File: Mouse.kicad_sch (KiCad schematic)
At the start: 0 parts

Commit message: putting onto other computers
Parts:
- added C1, C10, C11, C12, C13, C14, C4, C5, C6, C7, C8, C9: 100nF, symbol Device:C
- added R1, R2: 27.4, symbol Device:R
- added U1: RP2040, Package_DFN_QFN:QFN-56-1EP_7x7mm_P0.4mm_EP3.2x3.2mm, symbol MCU_RaspberryPi:RP2040
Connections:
- new net: R2.2, U1.46 (USB_DM)
- new net: R1.2, U1.47 (USB_DP)
- new net: U1.1 (IOVDD), U1.10 (IOVDD), U1.22 (IOVDD), U1.33 (IOVDD), U1.42 (IOVDD), U1.43 (ADC_AVDD), U1.44 (VREG_VIN), U1.48 (USB_VDD), U1.49 (IOVDD)
- new net: U1.23 (DVDD), U1.45 (VREG_VOUT), U1.50 (DVDD)
- new net +1V1: C10.1, C11.1, C12.1
- new net +3V3: C1.1, C13.1, C14.1, C4.1, C5.1, C6.1, C7.1, C8.1, C9.1
- new net ADC0: U1.38 (GPIO26/ADC0)
- new net ADC1: U1.39 (GPIO27/ADC1)
- new net ADC2: U1.40 (GPIO28/ADC2)
- new net ADC3: U1.41 (GPIO29/ADC3)
- new net GND: C1.2, C10.2, C11.2, C12.2, C13.2, C14.2, C4.2, C5.2, C6.2, C7.2, C8.2, C9.2, U1.57 (GND)
- new net I001: U1.3 (GPIO1)
- new net I002: U1.4 (GPIO2)
- new net IO00: U1.2 (GPIO0)
- new net IO03: U1.5 (GPIO3)
- new net IO04: U1.6 (GPIO4)
- new net IO05: U1.7 (GPIO5)
- new net IO06: U1.8 (GPIO6)
- new net IO07: U1.9 (GPIO7)
- new net IO08: U1.11 (GPIO8)
- new net IO09: U1.12 (GPIO9)
- new net IO10: U1.13 (GPIO10)
- new net IO11: U1.14 (GPIO11)
- new net IO12: U1.15 (GPIO12)
- new net IO13: U1.16 (GPIO13)
- new net IO14: U1.17 (GPIO14)
- new net IO15: U1.18 (GPIO15)
- new net IO16: U1.27 (GPIO16)
- new net IO17: U1.28 (GPIO17)
- new net IO18: U1.29 (GPIO18)
- new net IO19: U1.30 (GPIO19)
- new net IO20: U1.31 (GPIO20)
- new net IO21: U1.32 (GPIO21)
- new net IO22: U1.34 (GPIO22)
- new net IO23: U1.35 (GPIO23)
- new net IO24: U1.36 (GPIO24)
- new net IO25: U1.37 (GPIO25)
- new net QSPL_SCLK: U1.52 (QSPI_SCLK)
- new net QSPL_SD1: U1.55 (QSPI_SD1)
- new net QSPL_SD2: U1.54 (QSPI_SD2)
- new net QSPL_SD3: U1.51 (QSPI_SD3)
- new net QSPL_SDO: U1.53 (QSPI_SD0)
- new net QSPL_SS: U1.56 (~{QSPI_SS})
- new net RUN: U1.26 (RUN)
- new net SWCLK: U1.24 (SWCLK)
- new net SWDIO: U1.25 (SWDIO)
- new net TESTEN: U1.19 (TESTEN)
- new net XIN: U1.20 (XIN)
- new net XOUT: U1.21 (XOUT)

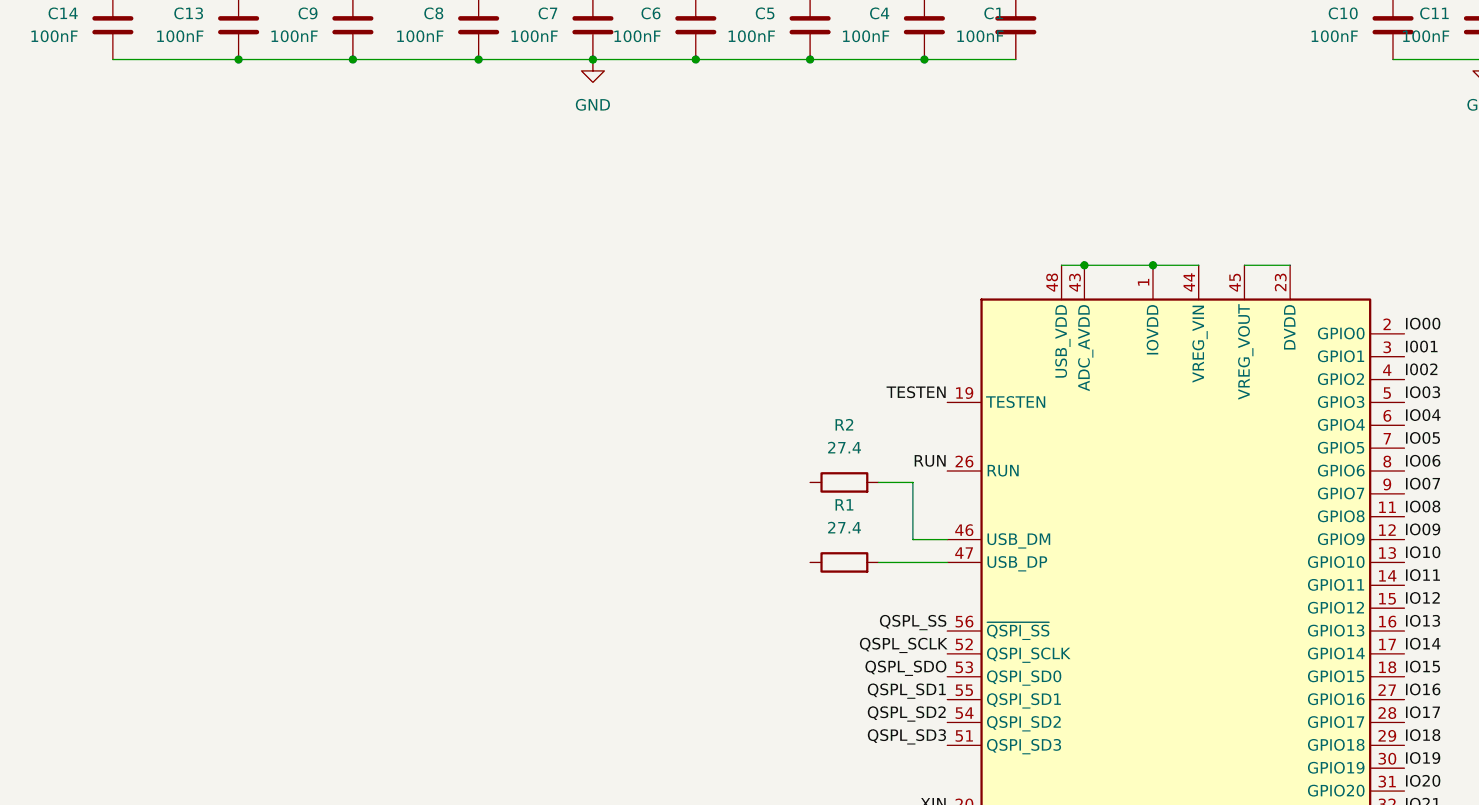
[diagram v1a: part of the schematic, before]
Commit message: added usb-C saved
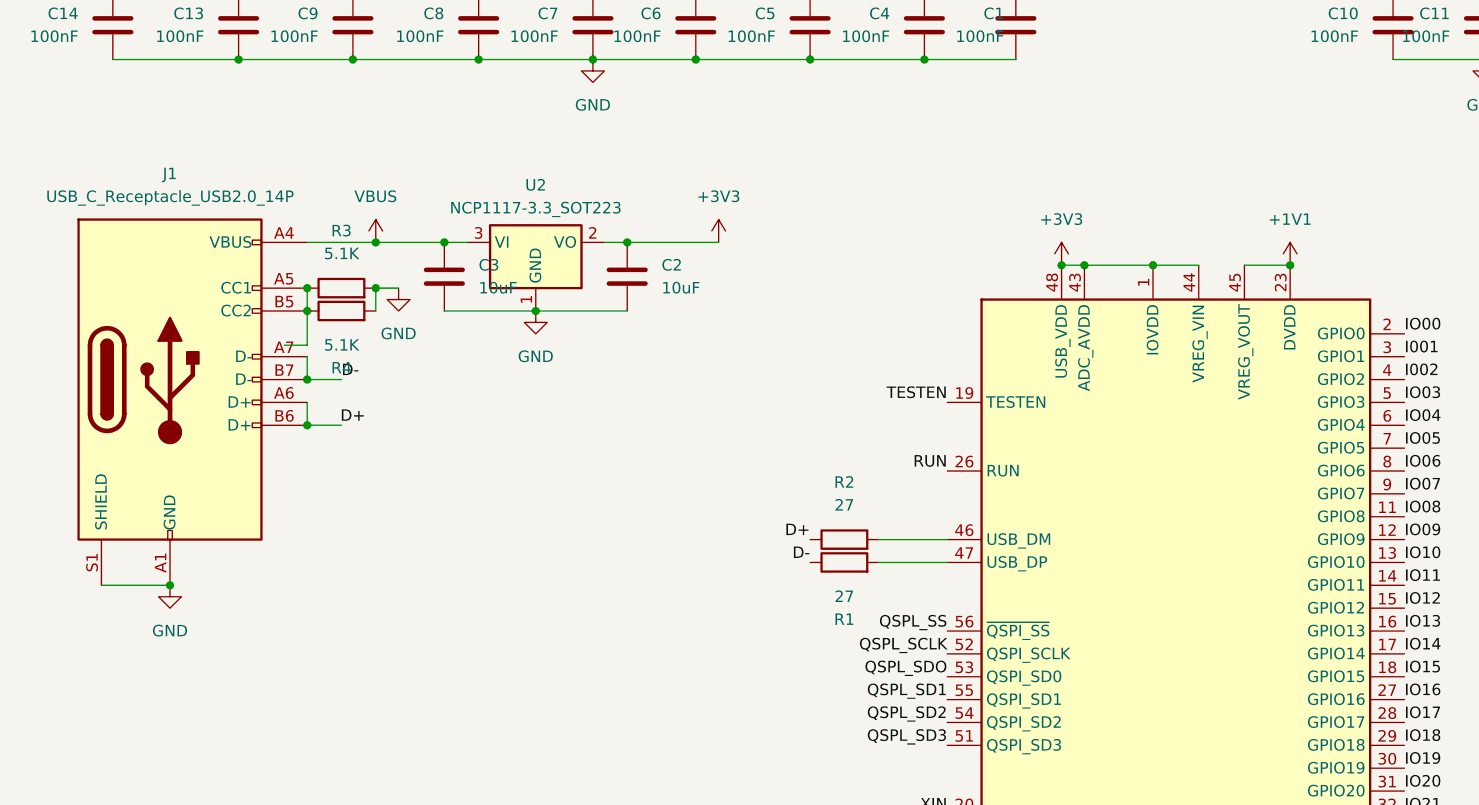
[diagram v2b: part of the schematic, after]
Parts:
- added C2, C3: 10uF, symbol Device:C
- added J1: USB_C_Receptacle_USB2.0_14P, symbol Connector:USB_C_Receptacle_USB2.0_14P
- added R3, R4: 5.1K, symbol Device:R
- added U2: NCP1117-3.3_SOT223, Package_TO_SOT_SMD:SOT-223-3_TabPin2, symbol Regulator_Linear:NCP1117-3.3_SOT223
- R1, R2: value 27.4 -> 27
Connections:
- net +1V1: now also U1.23 (DVDD), U1.45 (VREG_VOUT), U1.50 (DVDD)
- net +3V3: now also U1.1 (IOVDD), U1.10 (IOVDD), U1.22 (IOVDD), U1.33 (IOVDD), U1.42 (IOVDD), U1.43 (ADC_AVDD), U1.44 (VREG_VIN), U1.48 (USB_VDD), U1.49 (IOVDD), C2.1, U2.2 (VO)
- net GND: now also C2.2, C3.2, J1.A1 (GND), J1.A12 (GND), J1.B1 (GND), J1.B12 (GND), J1.S1 (SHIELD), R3.2, R4.2, U2.1 (GND)
- net D+: now reaches R2.1
- net D+: now also J1.A6 (D+), J1.B6 (D+)
- net D-: now reaches R1.1
- net D-: now also J1.A7 (D-), J1.B7 (D-)
- new net: J1.A5 (CC1), J1.B5 (CC2), R3.1, R4.1
- new net VBUS: C3.1, J1.A4 (VBUS), J1.A9 (VBUS), J1.B4 (VBUS), J1.B9 (VBUS), U2.3 (VI)
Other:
- moved on the sheet: R2

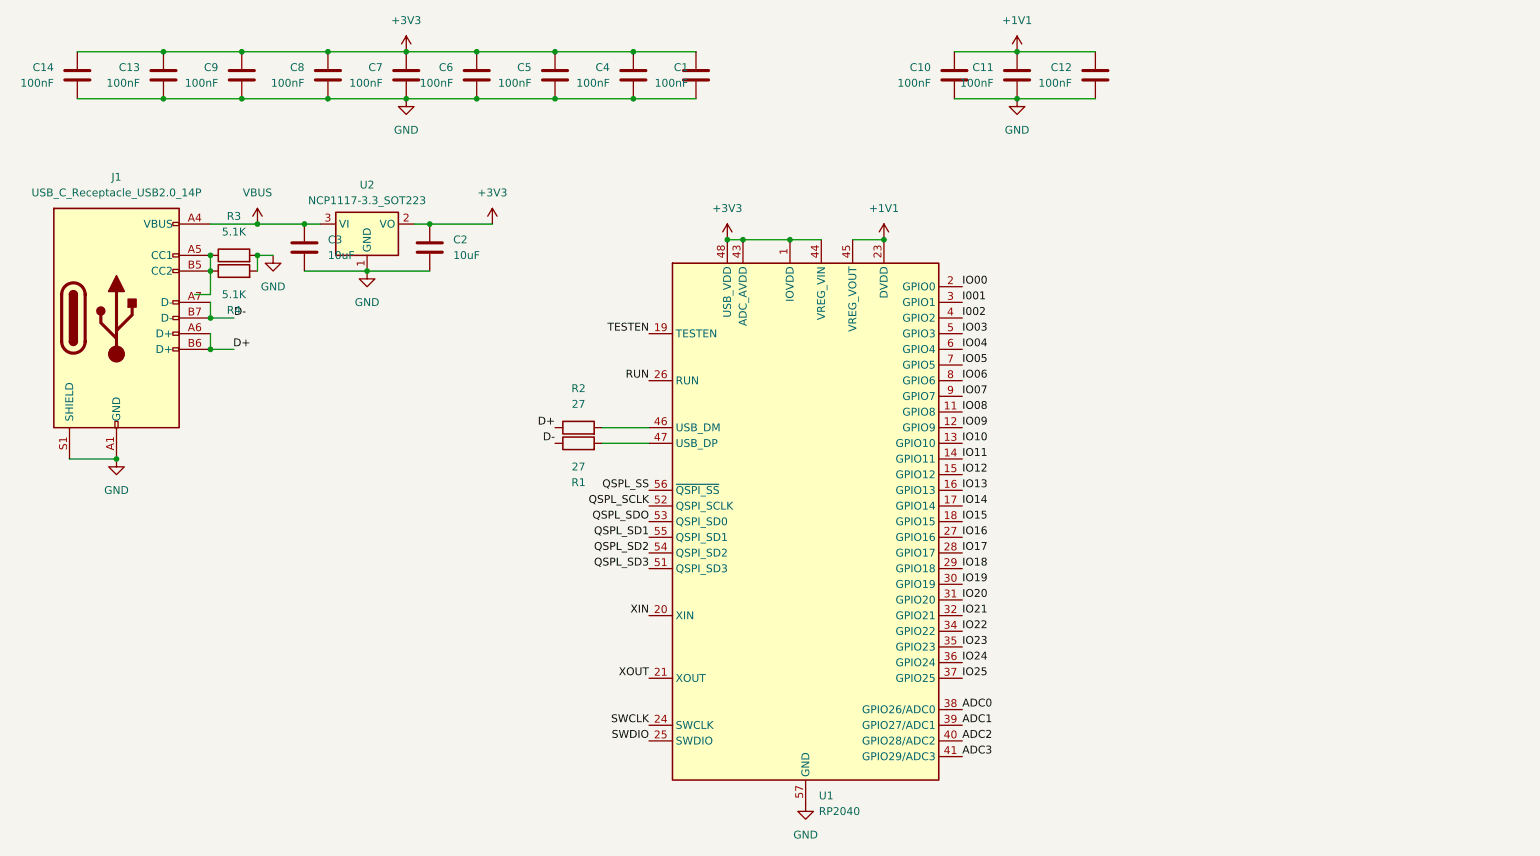
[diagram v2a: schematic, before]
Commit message: changed to esp32
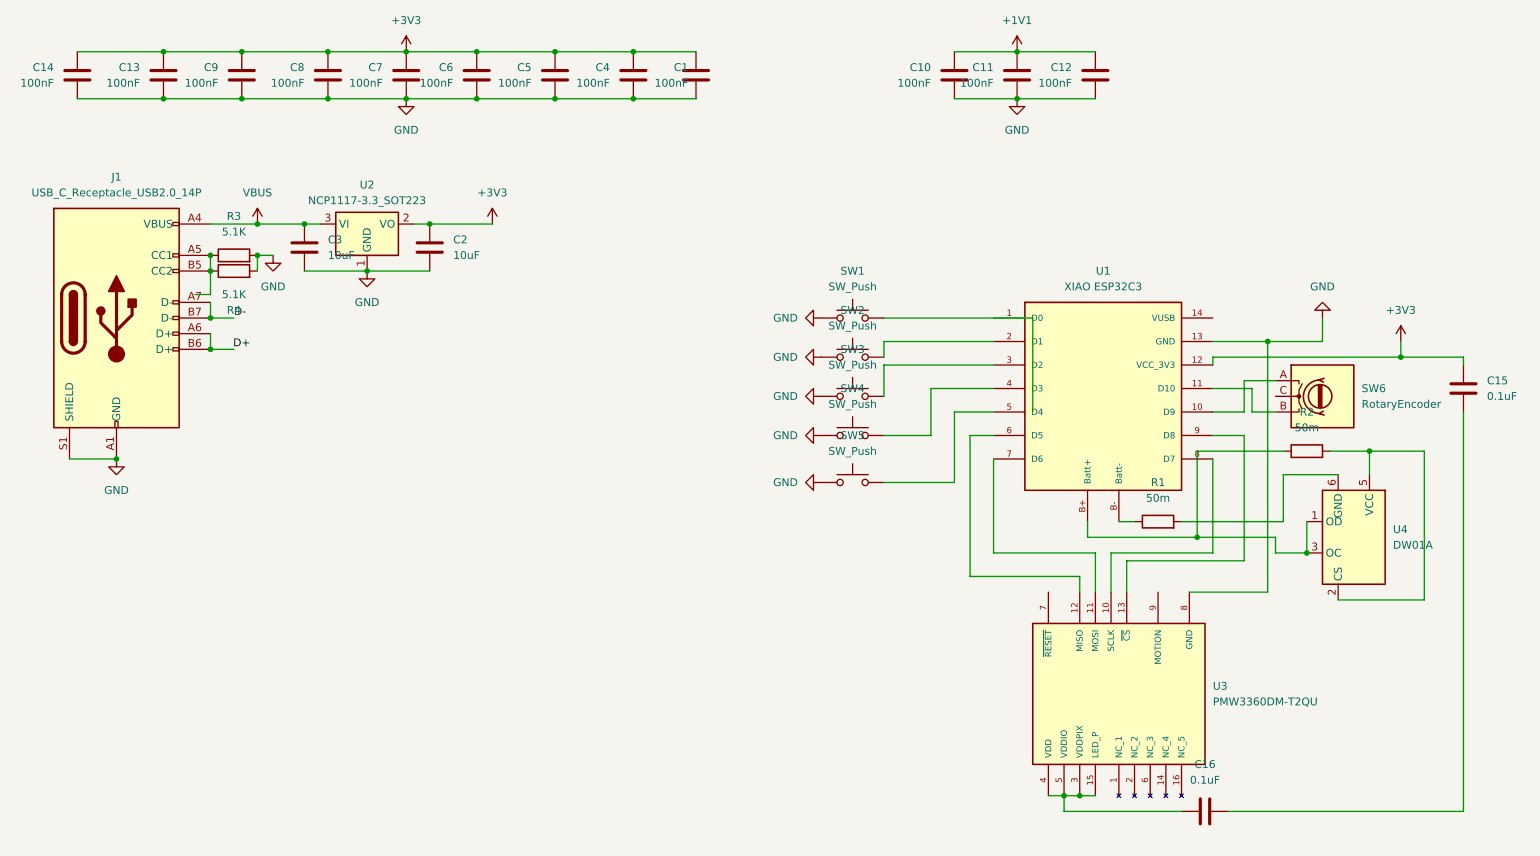
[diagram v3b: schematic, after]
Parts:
- removed U1: RP2040, Package_DFN_QFN:QFN-56-1EP_7x7mm_P0.4mm_EP3.2x3.2mm, symbol MCU_RaspberryPi:RP2040
- added C15, C16: 0.1uF, symbol Device:C
- added SW1, SW2, SW3, SW4, SW5: SW_Push, symbol Switch:SW_Push
- added SW6: RotaryEncoder, symbol Device:RotaryEncoder
- added U1: XIAO ESP32C3, XIAO_ESP32C3:xiao_esp32c3, symbol xiao_esp32c3:XIAO ESP32C3
- added U3: PMW3360DM-T2QU, Mouse Sensor:PMW3360DM-T2QU, symbol pmw3360dm-t2qu:PMW3360DM-T2QU
- added U4: DW01A, Package_TO_SOT_SMD:SOT-23-6, symbol Battery_Management:DW01A
- R1, R2: value 27 -> 50m
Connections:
- net +3V3: now also C15.1, U1.12 (VCC_3V3)
- net D+: no longer R2.1
- net D-: no longer R1.1
- net GND: now also SW1.1, SW2.1, SW3.1, SW4.1, SW5.1, U1.13 (GND), U3.8 (GND)
- net at R2.2: now also U4.2 (CS), U4.5 (VCC)
- net at R1.2: now also U4.6 (GND)
- new net: SW2.2, U1.2 (D1)
- new net: R1.1, U1.B- (Batt-)
- new net: C15.2, C16.1
- new net: C16.2, U3.15 (LED_P), U3.3 (VDDPIX), U3.4 (VDD), U3.5 (VDDIO)
- new net: SW6.A, U1.10 (D9)
- new net: SW6.B, U1.11 (D10)
- new net: SW5.2, U1.5 (D4)
- new net: SW3.2, U1.3 (D2)
- new net: SW4.2, U1.4 (D3)
- new net: R2.1, U1.B+ (Batt+), U4.1 (OD), U4.3 (OC)
- new net: U1.6 (D5), U3.12 (MISO)
- new net: U1.7 (D6), U3.11 (MOSI)
- new net: U1.8 (D7), U3.10 (SCLK)
- new net: U1.9 (D8), U3.13 (~{CS})
